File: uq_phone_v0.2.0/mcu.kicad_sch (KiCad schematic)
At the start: 42 parts, among them J6 Conn_ARM_SWD_TagConnect_TC2030, J7 559092474, J9 559092474, Q1 MMBT3904LP-7, Q2 MMBT3904LP-7, U17 TXU0204DTRR, U18 TXU0304DTRR, U19 TXU0104DTRR, U20 TXU0104DTRR, U21 STM32H723ZGI6, U5 TCA9509MRVHR

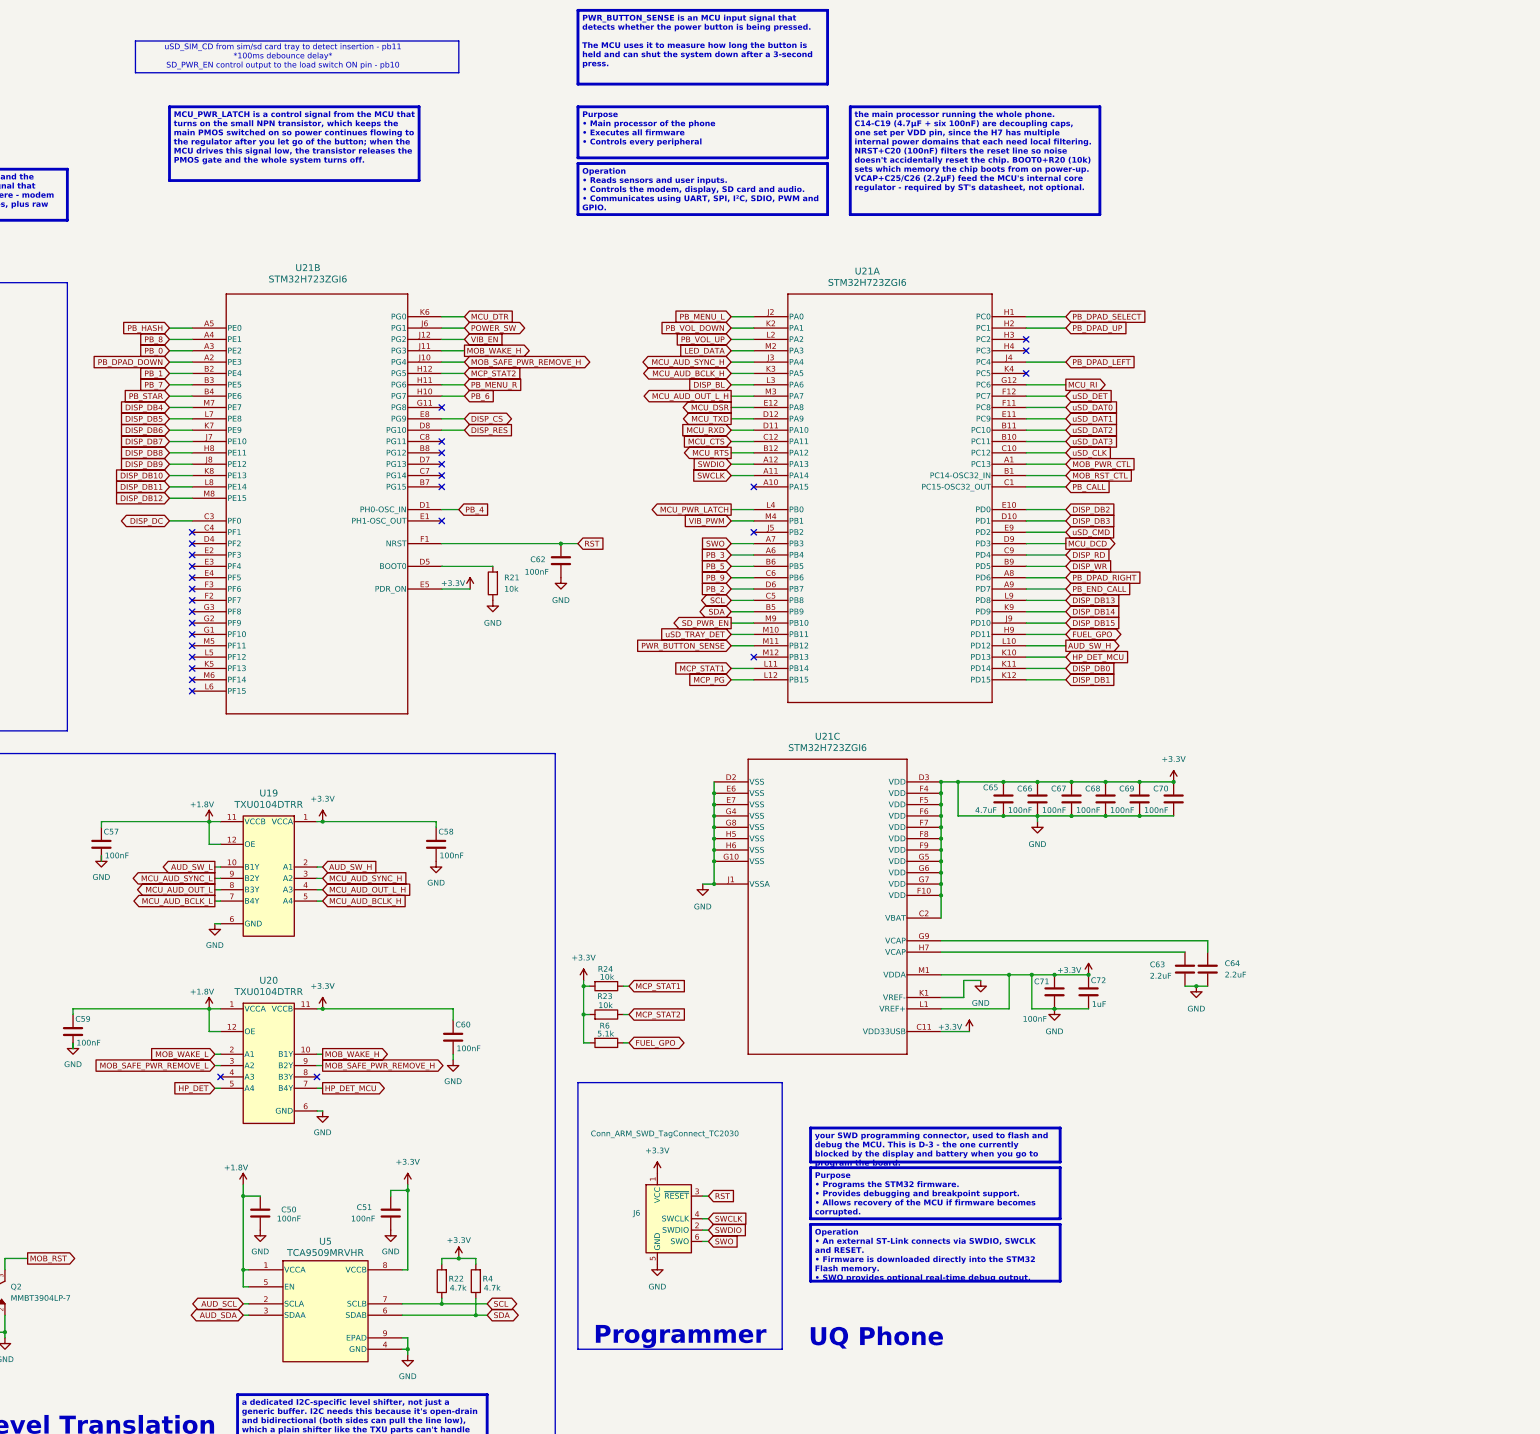
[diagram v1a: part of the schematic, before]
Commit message: Revert "Complete STM32H723ZGI6 144-pin schematic and FMC mapping"
This reverts commit c988dda79df5cbf87dce3ceded82a655262fe630.
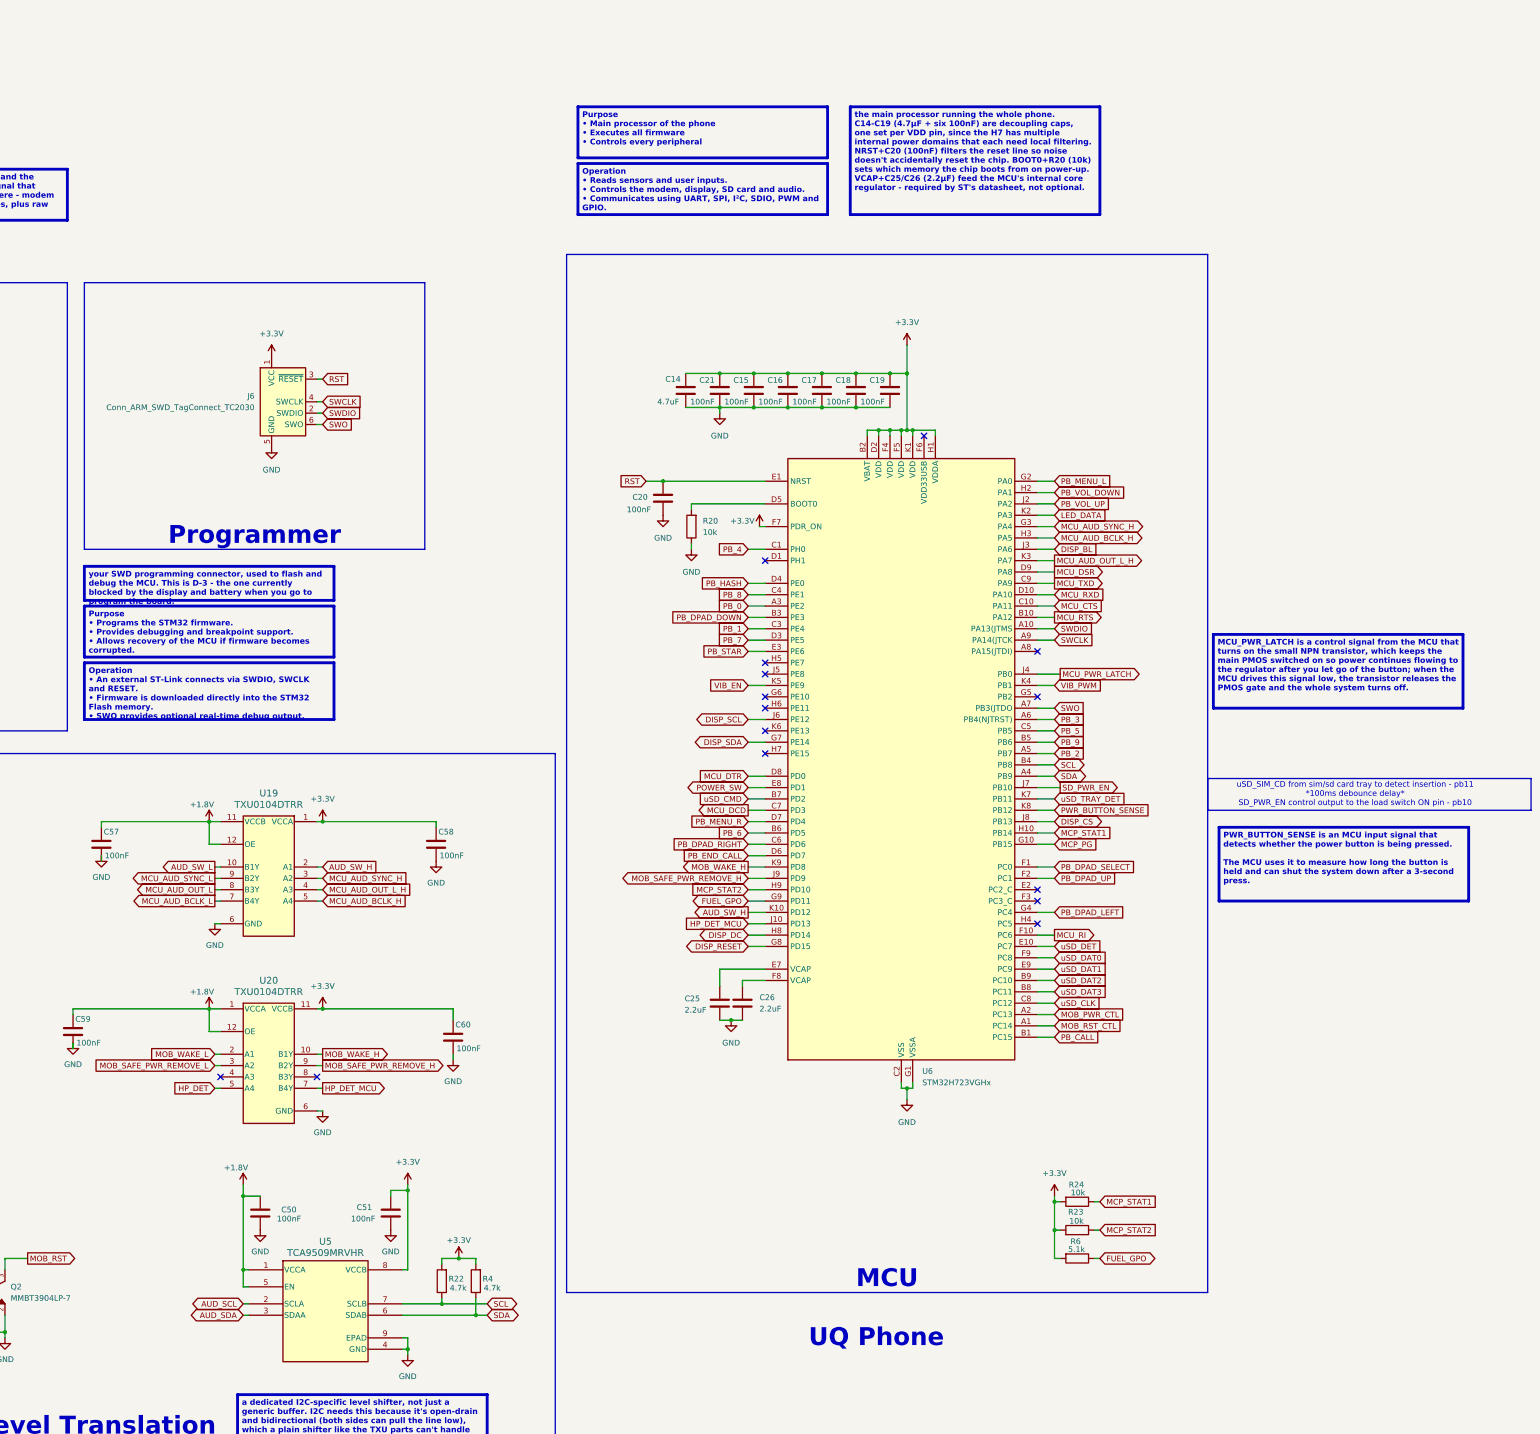
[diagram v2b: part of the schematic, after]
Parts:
- removed C62, C66, C67, C68, C69, C70, C71: 100nF, Capacitor_SMD:C_0201_0603Metric, symbol Capacitors:capacitor_100nF
- removed C63, C64: 2.2uF, Capacitor_SMD:C_0402_1005Metric, symbol Capacitors:Capacitor_2.2uF
- removed C65: 4.7uF, Capacitor_SMD:C_0201_0603Metric, symbol Capacitors:Capacitor_4.7uF
- removed C72: 1uF, Capacitor_SMD:C_0201_0603Metric, symbol Capacitors:Capacitor_1uF
- removed R21: 10k, Resistor_SMD:R_0201_0603Metric, symbol Resistors:Resistor_10k
- removed U21: STM32H723ZGI6, UFBGA-144_7X7_STM, symbol STM32H723ZGI6 UFBGA144:STM32H723ZGI6
- added C14: 4.7uF, Capacitor_SMD:C_0201_0603Metric, symbol Capacitors:Capacitor_4.7uF
- added C15, C16, C17, C18, C19, C20, C21: 100nF, Capacitor_SMD:C_0201_0603Metric, symbol Capacitors:capacitor_100nF
- added C25, C26: 2.2uF, Capacitor_SMD:C_0402_1005Metric, symbol Capacitors:Capacitor_2.2uF
- added R20: 10k, Resistor_SMD:R_0201_0603Metric, symbol Resistors:Resistor_10k
- added U6: STM32H723VGHx, Package_BGA:TFBGA-100_8x8mm_Layout10x10_P0.8mm, symbol MCU_ST_STM32H7:STM32H723VGHx
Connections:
- net +3.3V: now also C14.1, C15.2, C16.2, C17.2, C18.2, C19.2, C21.2, U6.B2 (VBAT), U6.D2 (VDD), U6.F4 (VDD), U6.F5 (VDD), U6.F7 (PDR_ON), U6.H1 (VDDA), U6.K1 (VDD); no longer C28.2, C50.2, C51.2, C54.2, C55.2, C56.2, C57.2, C58.2, C59.2, C60.2, J6.5 (GND), J7.1, J7.10, J7.11, J7.12, J7.2, J7.24, J7.3, J7.4, J7.5, J7.6, J7.7, J7.8, J7.9, J7.P1, J7.P2, J7.P3, J7.P4, J9.5, J9.6, J9.7, J9.8, J9.P1, J9.P2, J9.P3, J9.P4, Q1.2, Q2.2, R18.1, R19.1, U17.6 (GND), U18.6 (GND), U19.6 (GND), U20.6 (GND), U5.4 (GND), U5.9 (EPAD)
- net AUD_SW_H: now also U6.K10 (PD12)
- net DISP_BL: now also U6.J3 (PA6)
- net DISP_CS: now also U6.J8 (PB13)
- net DISP_DC: now also U6.H8 (PD14)
- net FUEL_GPO: now also U6.G9 (PD11)
- net HP_DET_MCU: now also U6.J10 (PD13)
- net LED_DATA: now also U6.K2 (PA3)
- net MCP_PG: now also U6.G10 (PB15)
- net MCP_STAT1: now also U6.H10 (PB14)
- net MCP_STAT2: now also U6.H9 (PD10)
- net MCU_AUD_BCLK_H: now also U6.H3 (PA5)
- net MCU_AUD_OUT_L_H: now also U6.K3 (PA7)
- net MCU_AUD_SYNC_H: now also U6.G3 (PA4)
- net MCU_CTS: now also U6.C10 (PA11)
- net MCU_DCD: now also U6.C7 (PD3)
- net MCU_DSR: now also U6.D9 (PA8)
- net MCU_DTR: now also U6.D8 (PD0)
- net MCU_PWR_LATCH: now also U6.J4 (PB0)
- net MCU_RI: now also U6.F10 (PC6)
- net MCU_RTS: now also U6.B10 (PA12)
- net MCU_RXD: now also U6.D10 (PA10)
- net MCU_TXD: now also U6.C9 (PA9)
- net MOB_PWR_CTL: now also U6.A2 (PC13)
- net MOB_RST_CTL: now also U6.A1 (PC14)
- net MOB_SAFE_PWR_REMOVE_H: now also U6.J9 (PD9)
- net MOB_WAKE_H: now also U6.K9 (PD8)
- net PB_0: now also U6.A3 (PE2)
- net PB_1: now also U6.C3 (PE4)
- net PB_2: now also U6.A5 (PB7)
- net PB_3: now also U6.A6 (PB4(NJTRST))
- net PB_4: now also U6.C1 (PH0)
- net PB_5: now also U6.C5 (PB5)
- net PB_6: now also U6.B6 (PD5)
- net PB_7: now also U6.D3 (PE5)
- net PB_8: now also U6.C4 (PE1)
- net PB_9: now also U6.B5 (PB6)
- net PB_CALL: now also U6.B1 (PC15)
- net PB_DPAD_DOWN: now also U6.B3 (PE3)
- net PB_DPAD_LEFT: now also U6.G4 (PC4)
- net PB_DPAD_RIGHT: now also U6.C6 (PD6)
- net PB_DPAD_SELECT: now also U6.F1 (PC0)
- net PB_DPAD_UP: now also U6.F2 (PC1)
- net PB_END_CALL: now also U6.D6 (PD7)
- net PB_HASH: now also U6.D4 (PE0)
- net PB_MENU_L: now also U6.G2 (PA0)
- net PB_MENU_R: now also U6.D7 (PD4)
- net PB_STAR: now also U6.E3 (PE6)
- net PB_VOL_DOWN: now also U6.H2 (PA1)
- net PB_VOL_UP: now also U6.J2 (PA2)
- net POWER_SW: now also U6.E8 (PD1)
- net PWR_BUTTON_SENSE: now also U6.K8 (PB12)
- net RST: now also C20.2, U6.E1 (NRST)
- net SCL: now also U6.B4 (PB8)
- net SDA: now also U6.A4 (PB9)
- net SD_PWR_EN: now also U6.J7 (PB10)
- net SWCLK: now also U6.A9 (PA14(JTCK)
- net SWDIO: now also U6.A10 (PA13(JTMS)
- net SWO: now also U6.A7 (PB3(JTDO)
- net VIB_EN: now also U6.K5 (PE9)
- net VIB_PWM: now also U6.K4 (PB1)
- net uSD_CLK: now also U6.C8 (PC12)
- net uSD_CMD: now also U6.B7 (PD2)
- net uSD_DAT0: now also U6.F9 (PC8)
- net uSD_DAT1: now also U6.E9 (PC9)
- net uSD_DAT2: now also U6.B9 (PC10)
- net uSD_DAT3: now also U6.B8 (PC11)
- net uSD_DET: now also U6.E10 (PC7)
- net uSD_TRAY_DET: now also U6.K7 (PB11)
- new net: C26.1, U6.F8 (VCAP)
- new net: R20.2, U6.D5 (BOOT0)
- new net: C25.1, U6.E7 (VCAP)
- new net DISP_RESET: U6.G8 (PD15)
- new net DISP_SCL: U6.J6 (PE12)
- new net DISP_SDA: U6.G7 (PE14)
- new net GND: C14.2, C15.1, C16.1, C17.1, C18.1, C19.1, C20.1, C21.1, C25.2, C26.2, C28.2, C50.2, C51.2, C54.2, C55.2, C56.2, C57.2, C58.2, C59.2, C60.2, J6.5 (GND), J7.1, J7.10, J7.11, J7.12, J7.2, J7.24, J7.3, J7.4, J7.5, J7.6, J7.7, J7.8, J7.9, J7.P1, J7.P2, J7.P3, J7.P4, J9.5, J9.6, J9.7, J9.8, J9.P1, J9.P2, J9.P3, J9.P4, Q1.2, Q2.2, R18.1, R19.1, R20.1, U17.6 (GND), U18.6 (GND), U19.6 (GND), U20.6 (GND), U5.4 (GND), U5.9 (EPAD), U6.C2 (VSS), U6.E4 (VSS), U6.E5 (VSS), U6.E6 (VSS), U6.G1 (VSSA), U6.J1 (VSS)
- no-connect marks 30 -> 15
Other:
- moved on the sheet: J6, R23, R24, R6
